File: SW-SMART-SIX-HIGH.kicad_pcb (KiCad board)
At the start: 2 copper layers, 107.7 x 76.2 mm, 98 parts, among them J1 SWD, J2 USART2, J3 POWER OUT, J4 POWER IN, J5 POWER OUT, SW0 BTS7002-1EPP, SW1 BTS7002-1EPP, SW2 BTS7002-1EPP, SW3 BTS7002-1EPP, SW4 BTS7002-1EPP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

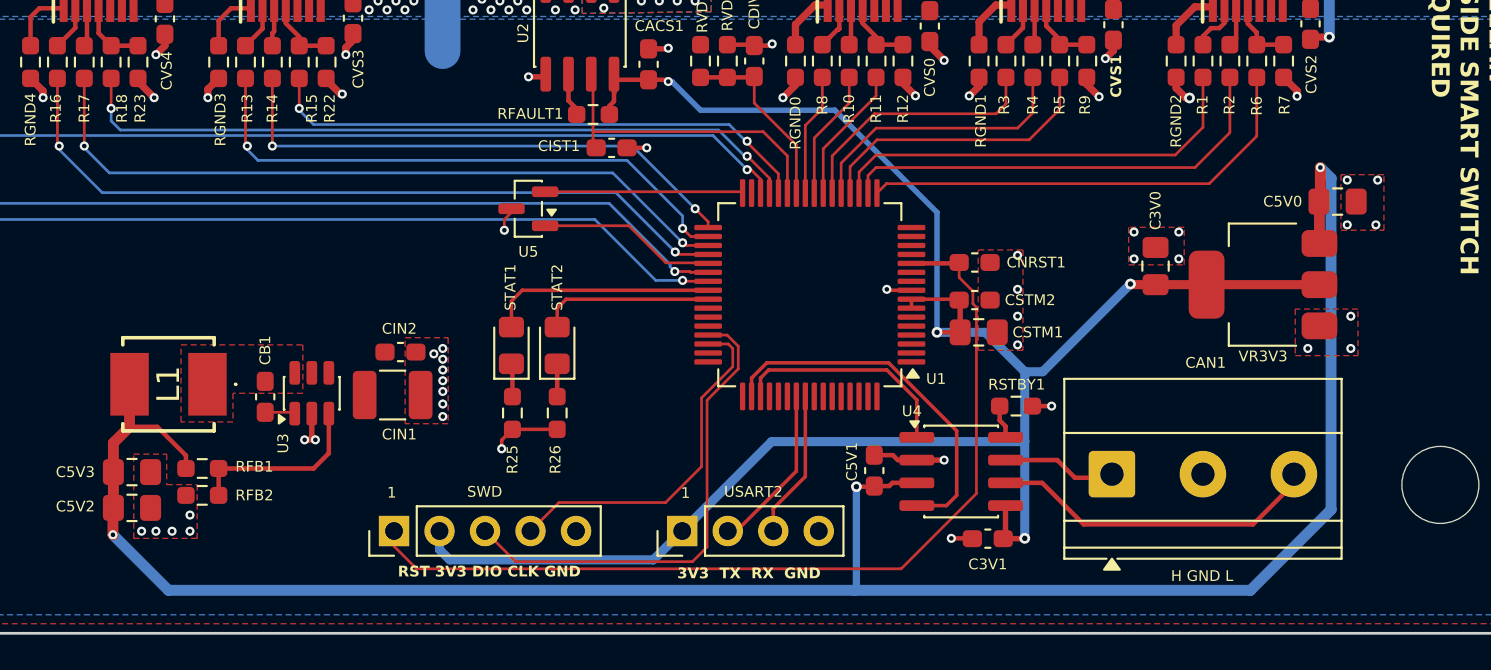
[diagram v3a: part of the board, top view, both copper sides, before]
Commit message: added dedicated board temp sensor and some silkscreen tweaks
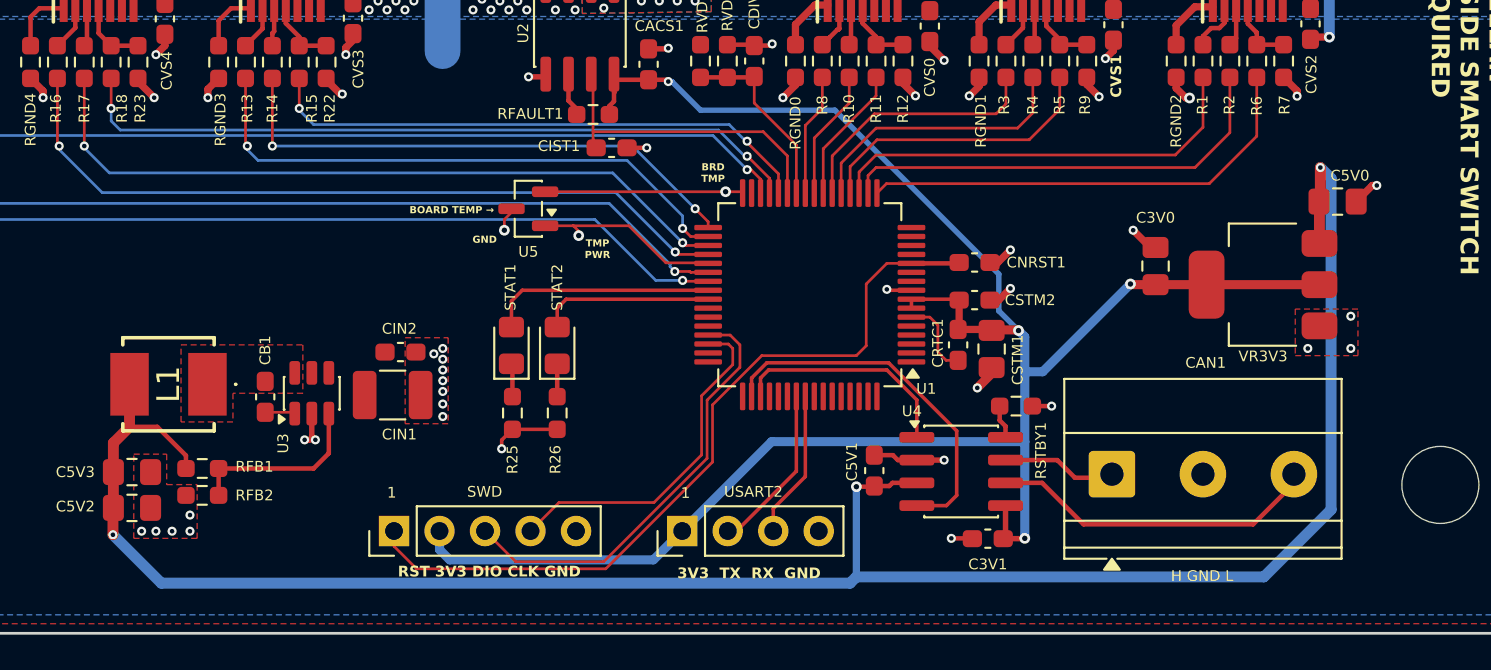
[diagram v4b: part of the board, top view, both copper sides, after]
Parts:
- added CRTC1: 100n, Capacitor_SMD:C_0603_1608Metric_Pad1.08x0.95mm_HandSolder, F.Cu at (125.3, 82.6)
- moved CSTM1 1.18 mm to (127.2, 82.8), turned to -90 degrees
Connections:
- U1 pad 6: unconnected-(U1-VBAT-Pad6) -> /RTC
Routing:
- net /NRST: track 51.5 -> 43.8 mm
- net GND: track 173.7 -> 180.4 mm, vias 66 -> 59
- net /RTC: track 0.00 -> 4.48 mm
- net /SWDIO: track 27.3 -> 24.6 mm
- net +5V: track 117.2 -> 116.0 mm
- net /TMP_PWR: track 9.97 -> 10.6 mm, vias 0 -> 1
- net /BRDTMP: track 11.1 -> 10.9 mm, vias 0 -> 1
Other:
- board text added: "BOARD TEMP →"
- board text added: "BRD TMP"
- board text added: "GND"
- board text added: "TMP PWR"

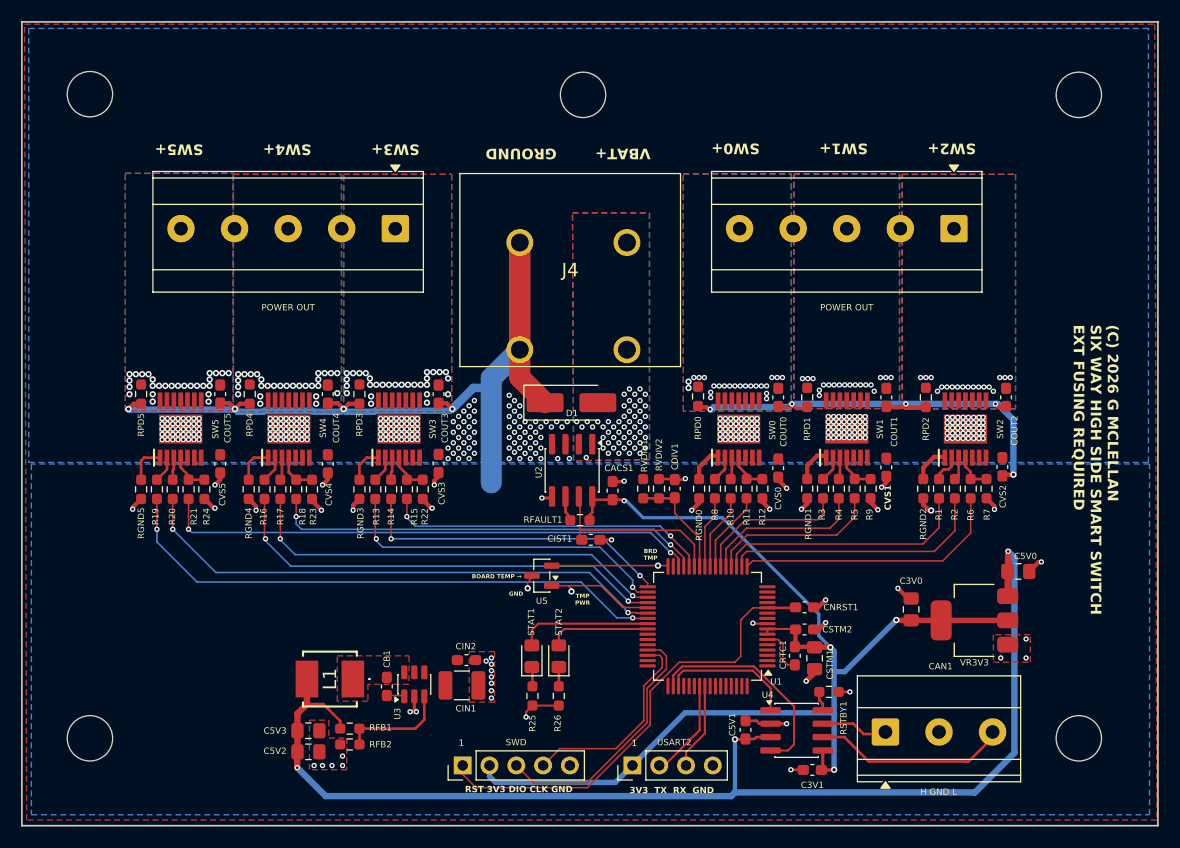
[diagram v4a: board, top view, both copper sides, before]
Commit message: changed can connector wiring and footprint size
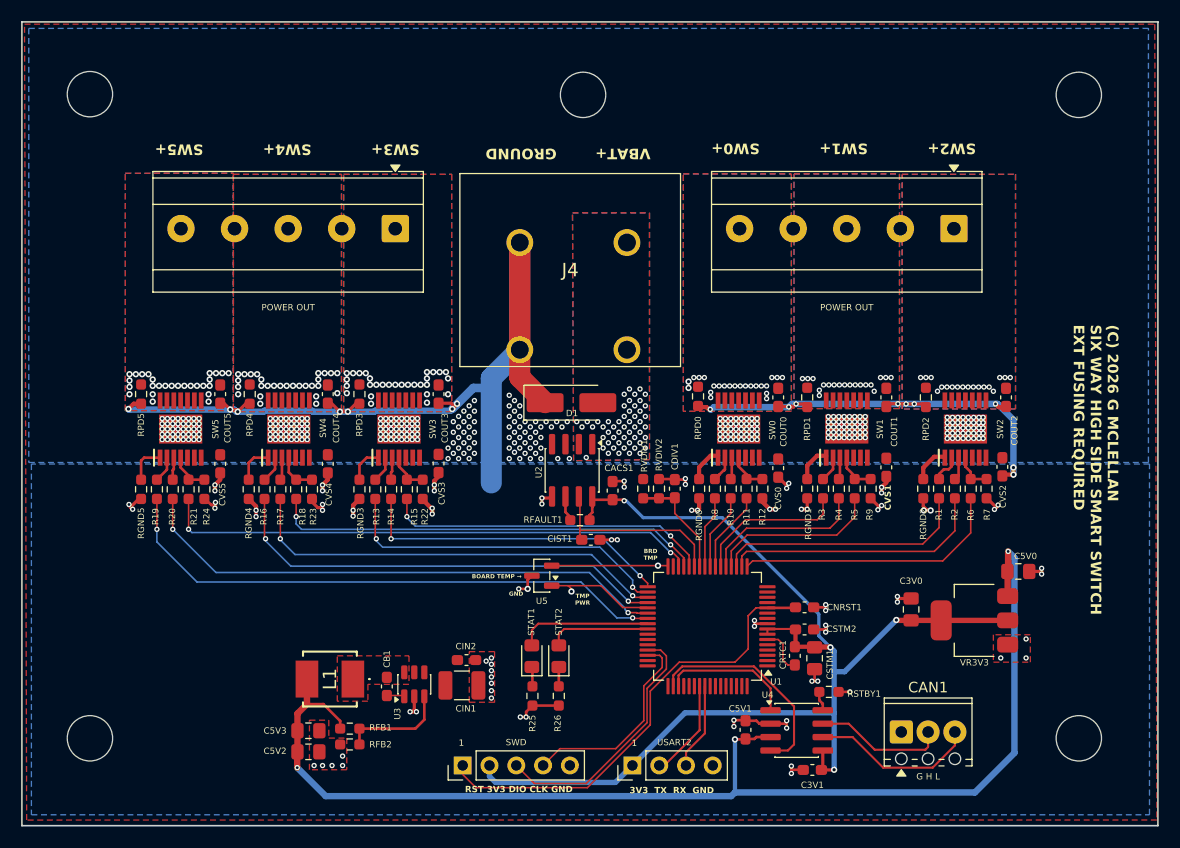
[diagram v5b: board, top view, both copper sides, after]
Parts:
- CAN1: value H GND L -> G H L; footprint TerminalBlock_Phoenix:TerminalBlock_Phoenix_MKDS-1,5-3-5.08_1x03_P5.08mm_Horizontal -> TerminalBlock_Phoenix:TerminalBlock_Phoenix_MPT-0,5-3-2.54_1x03_P2.54mm_Horizontal
- moved CAN1 1.50 mm to (135.4, 89.8)
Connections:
- CAN1 pad 1: /CAN_H -> GND
- CAN1 pad 2: GND -> /CAN_H
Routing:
- net GND: track 180.4 -> 200.1 mm, vias 59 -> 99
- net /CAN_H: track 6.15 -> 12.5 mm
- net /CAN_L: track 18.0 -> 15.9 mm

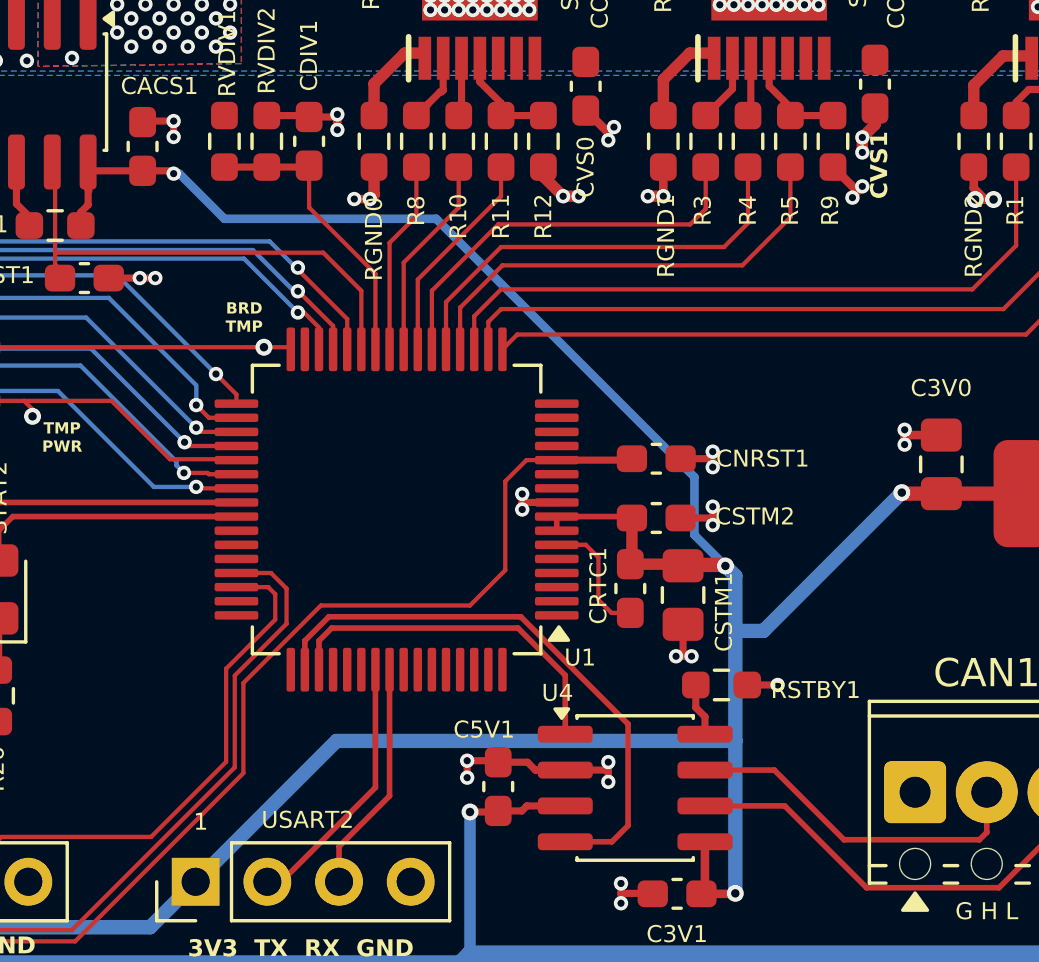
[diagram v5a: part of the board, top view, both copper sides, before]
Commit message: added recommended mcu vref capacitors
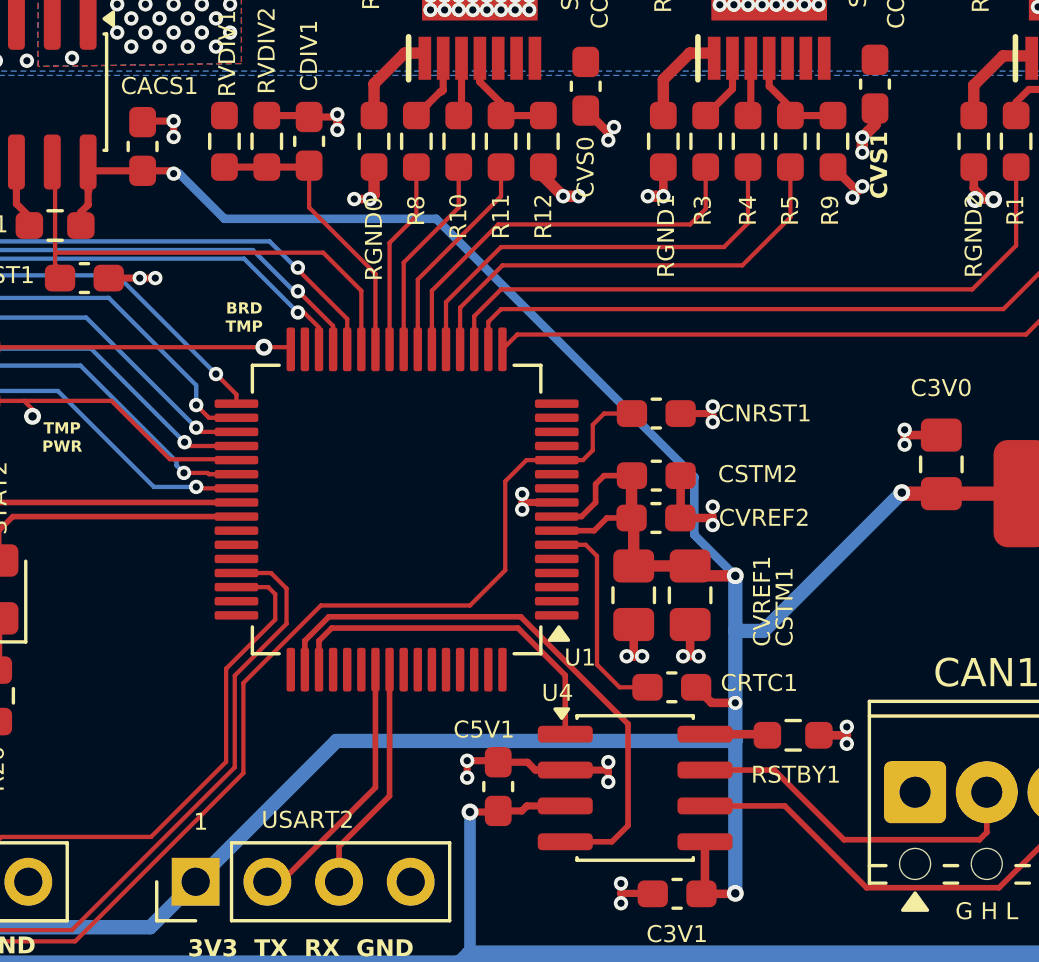
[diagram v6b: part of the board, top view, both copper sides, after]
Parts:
- added CVREF1: 1u, Capacitor_SMD:C_0805_2012Metric_Pad1.18x1.45mm_HandSolder, F.Cu at (125.5, 82.8)
- added CVREF2: 100n, Capacitor_SMD:C_0603_1608Metric_Pad1.08x0.95mm_HandSolder, F.Cu at (126.2, 80.1)
- moved CRTC1 3.80 mm to (126.8, 86.1), turned to 180 degrees
- moved RSTBY1 3.10 mm to (131.1, 87.8)
- moved CNRST1 1.60 mm to (126.2, 76.4)
- moved CSTM2 1.50 mm to (126.2, 78.6)
- moved CSTM1 0.25 mm to (127.5, 82.8)
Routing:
- net +3.3V: track 109.6 -> 116.7 mm, vias 4 -> 5
- net GND: track 200.1 -> 203.8 mm, vias 99 -> 102
- net /RTC: track 4.48 -> 7.56 mm
- net /NRST: track 43.6 -> 44.9 mm

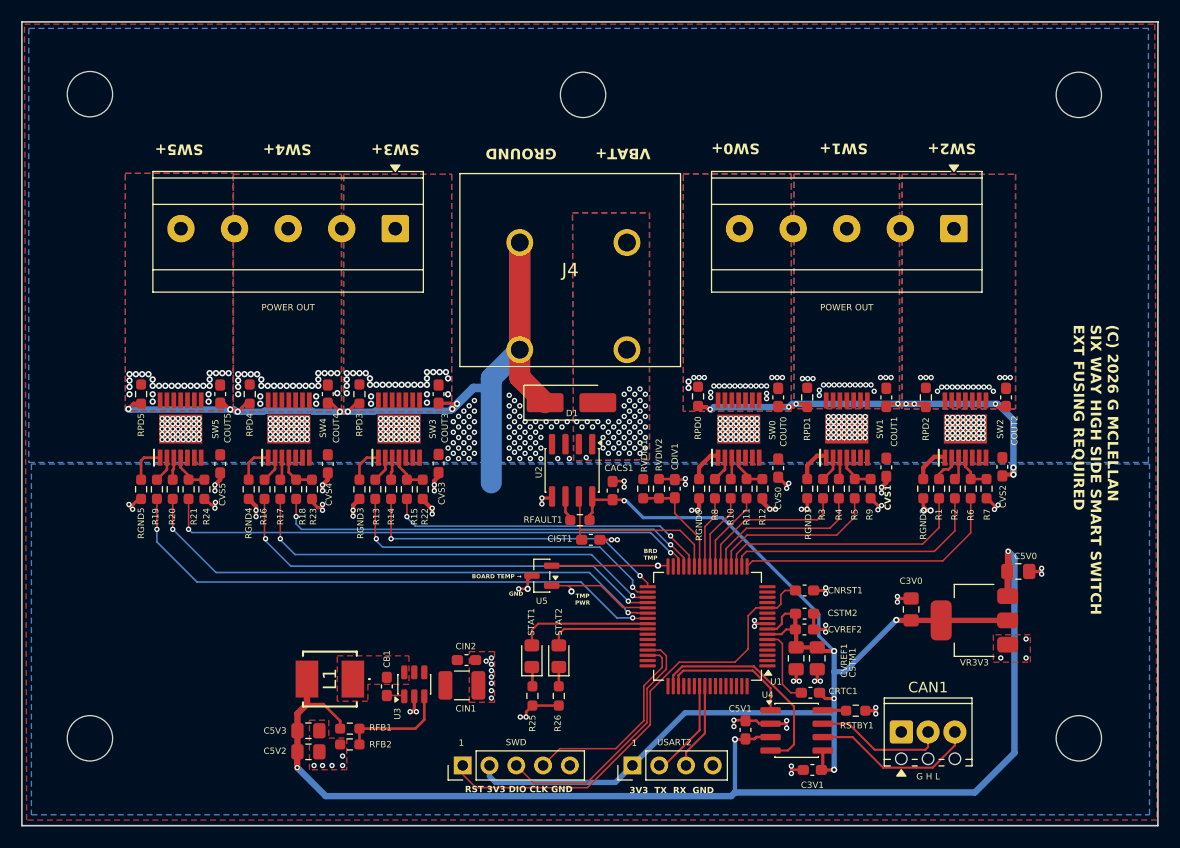
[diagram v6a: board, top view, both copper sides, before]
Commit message: adjusted grounding and copper pour dimensions
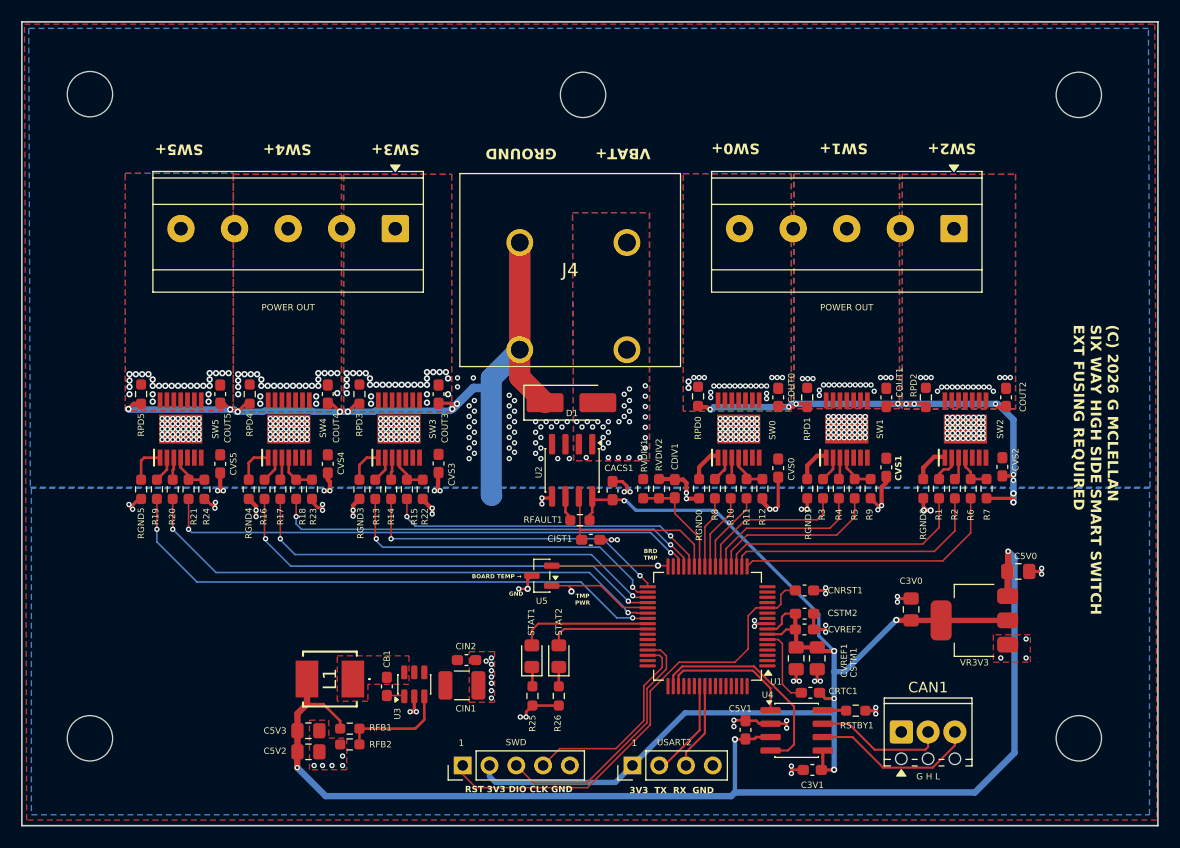
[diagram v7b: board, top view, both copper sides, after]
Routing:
- net GND: track 203.8 -> 212.2 mm, vias 102 -> 96
- net +3.3V: track 116.7 -> 116.0 mm
- net /VBAT: vias 52 -> 31
- net +12V: vias 310 -> 283

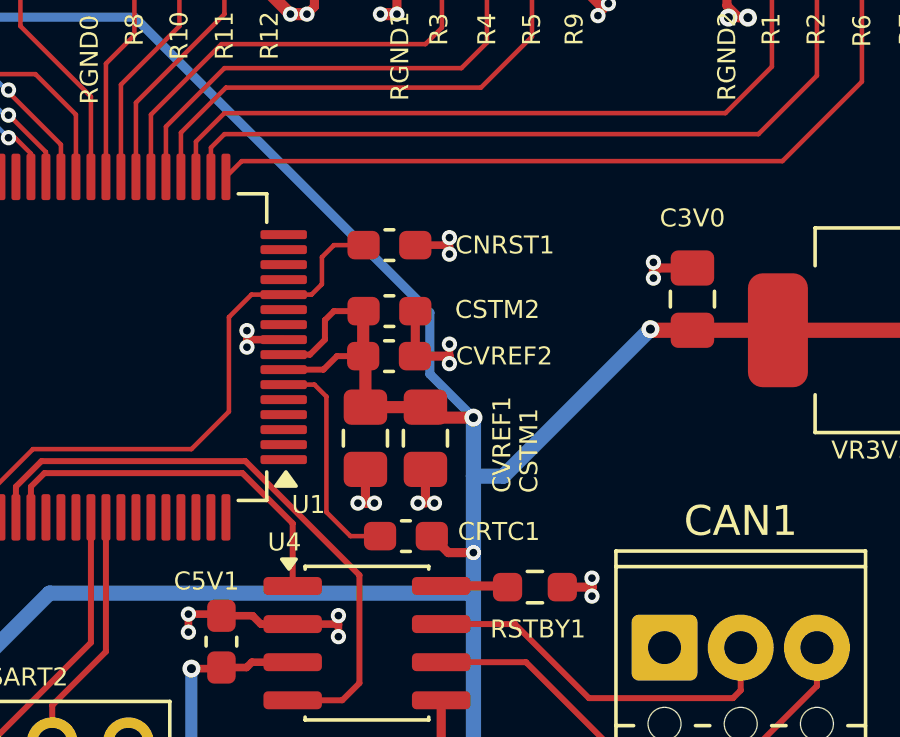
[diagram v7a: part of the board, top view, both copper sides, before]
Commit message: added crystal osc
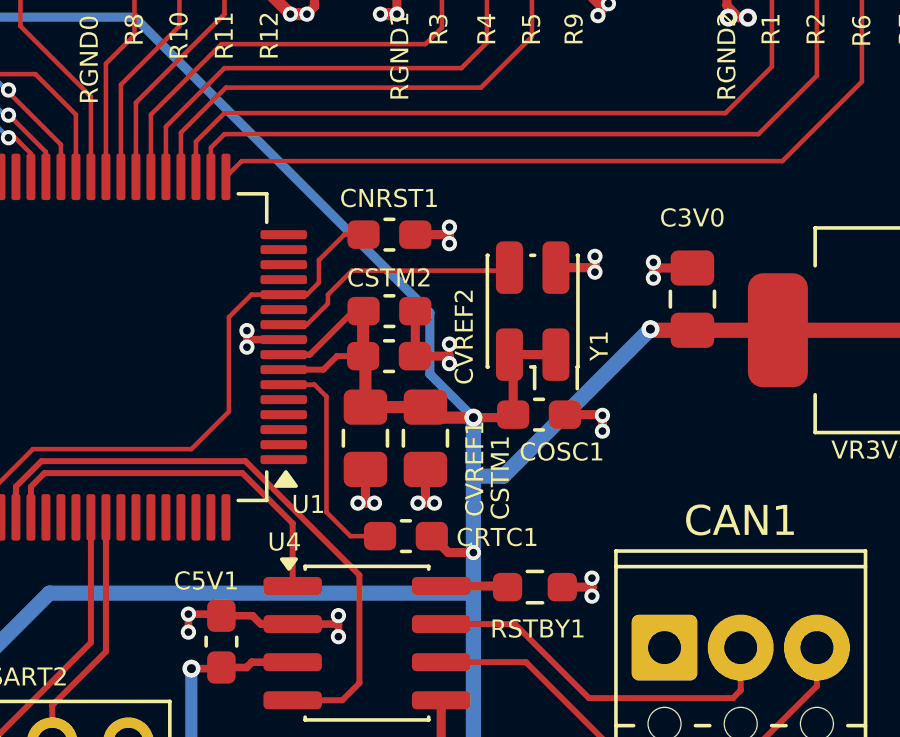
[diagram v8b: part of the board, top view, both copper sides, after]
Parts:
- added COSC1: 100n, Capacitor_SMD:C_0603_1608Metric_Pad1.08x0.95mm_HandSolder, F.Cu at (131.2, 82.0)
- added Y1: 8MHz, Oscillator:Oscillator_SMD_EuroQuartz_XO32-4Pin_3.2x2.5mm_RotB_HandSoldering, F.Cu at (131.0, 78.6)
- moved CNRST1 0.35 mm to (126.2, 76.0)
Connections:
- U1 pad 10: unconnected-(U1-PF0-Pad10) -> /OSC
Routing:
- net /OSC: track 0.00 -> 8.49 mm
- net +3.3V: track 116.0 -> 120.6 mm
- net GND: track 212.2 -> 216.0 mm, vias 96 -> 100
